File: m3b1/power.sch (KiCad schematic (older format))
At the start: 14 parts, among them U1 MC307, U10 MC309, U11 MC310, U12 MC309, U2 MC306, U3 MC306, U4 MC306, U5 MC302, U6 MC306, U7 MC301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

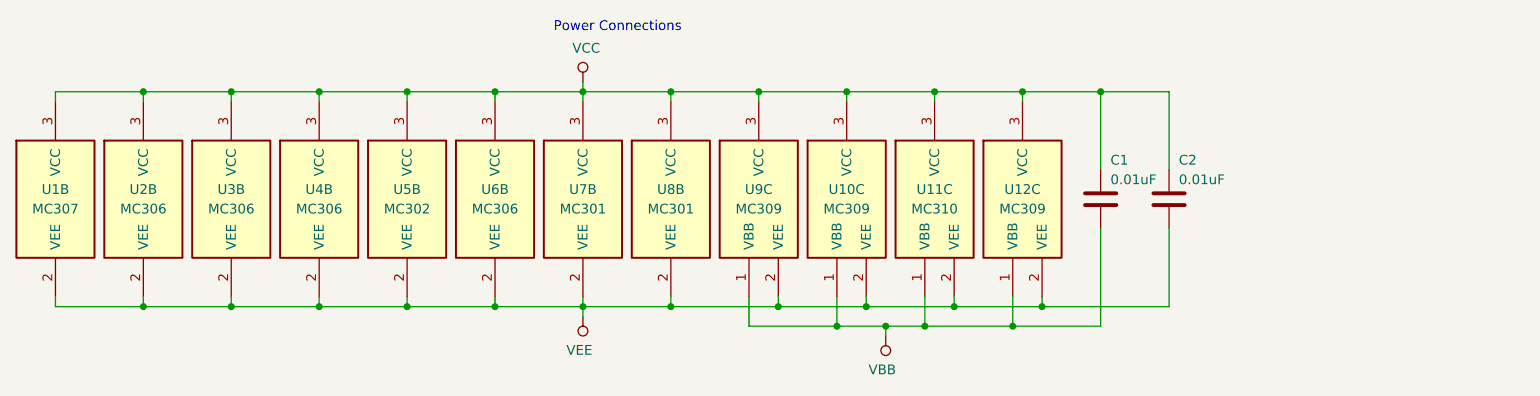
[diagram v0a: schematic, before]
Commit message: Greatly cleaned up all of the schematics so far; everything passes DRC.
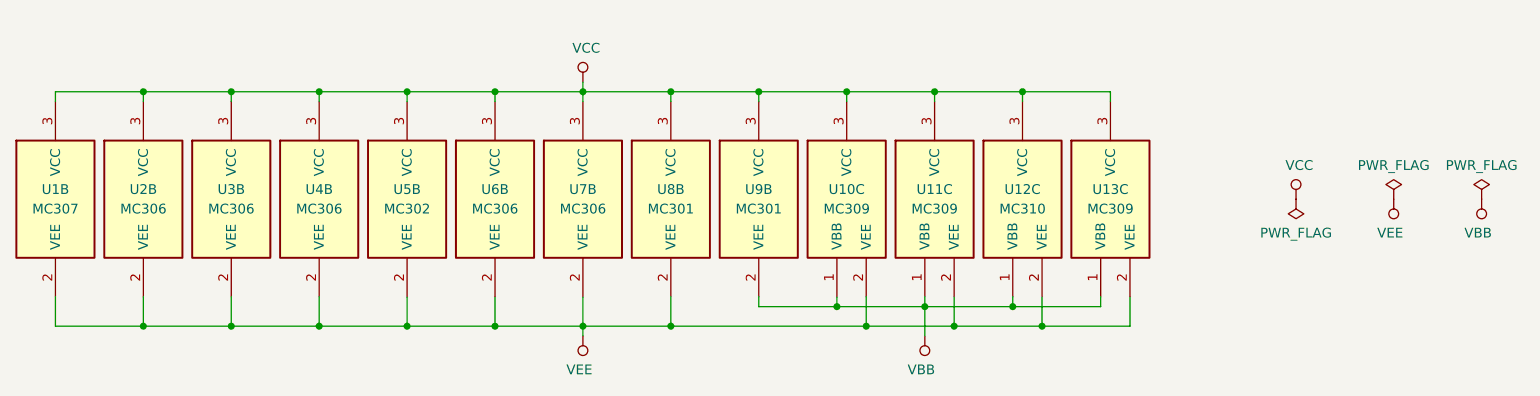
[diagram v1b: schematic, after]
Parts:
- removed C1, C2: 0.01uF, symbol Device:C
- removed U11: MC310, symbol gn_buffer:MC310
- removed U12, U9: MC309, symbol gn_buffer:MC309
- removed U7: MC301, symbol gn_buffer:MC301
- added U11, U13: MC309, symbol gn_buffer:MC309
- added U12: MC310, symbol gn_buffer:MC310
- added U7: MC306, symbol gn_buffer:MC306
- added U9: MC301, symbol gn_buffer:MC301
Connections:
- net VBB: now also U11.1 (VBB), U12.1 (VBB), U13.1 (VBB), U9.2 (VEE)
- net VCC: now also U11.3 (VCC), U12.3 (VCC), U13.3 (VCC), U7.3 (VCC), U9.3 (VCC)
- net VEE: now also U11.2 (VEE), U12.2 (VEE), U13.2 (VEE), U7.2 (VEE)
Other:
- note removed: "Power Connections"
